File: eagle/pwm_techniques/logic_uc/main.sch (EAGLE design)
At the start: 32 parts, among them IC1 7805T, U1 SN74LS08D, U2 SN74HCT04D

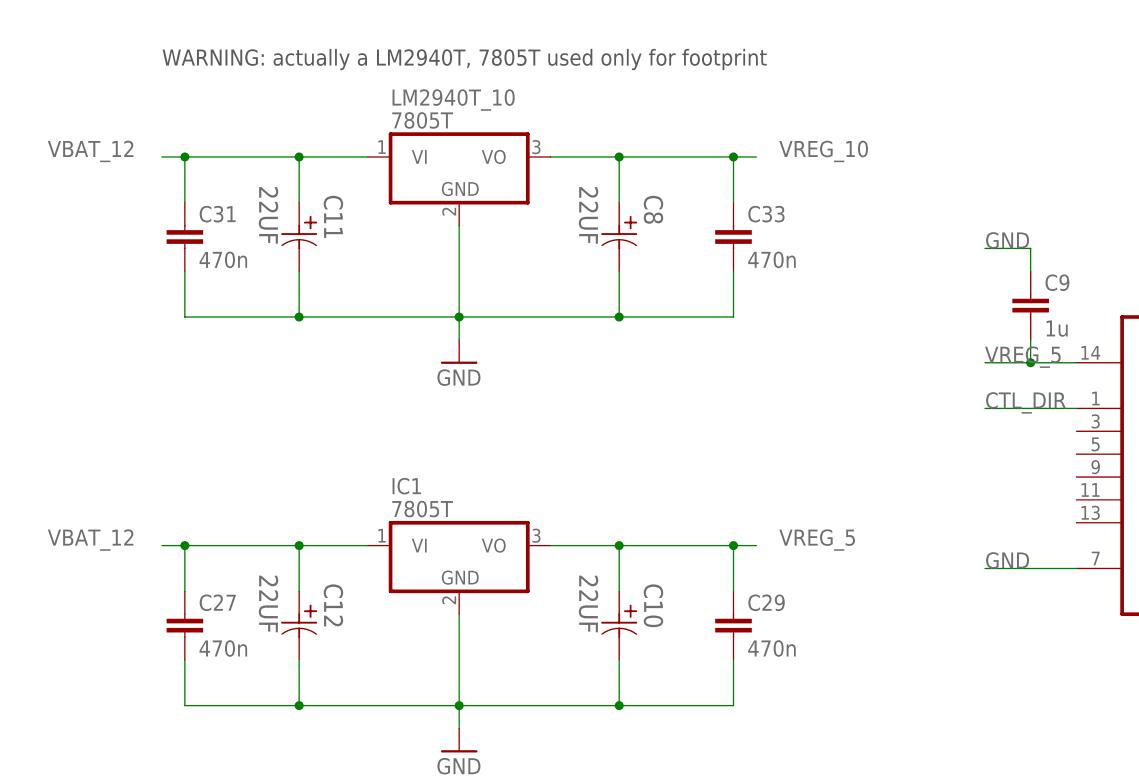
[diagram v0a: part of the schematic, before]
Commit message: [ update ] use SOT223 for LDOs
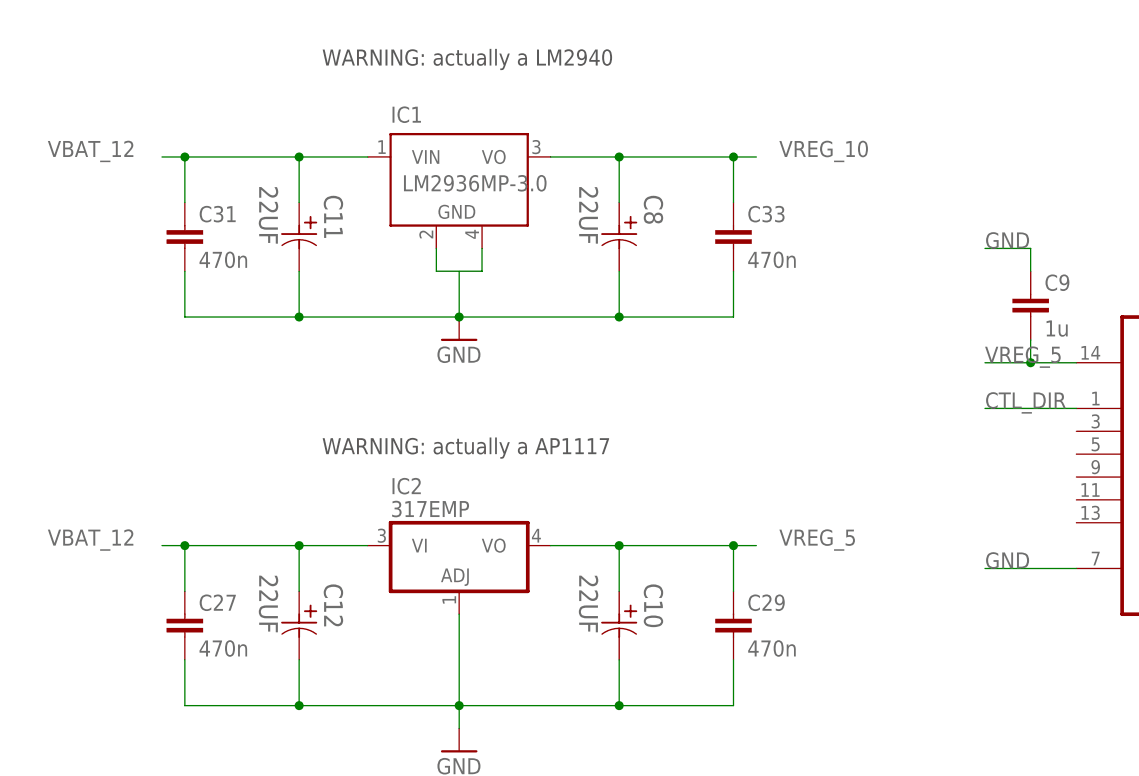
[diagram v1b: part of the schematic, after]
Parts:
- removed LM2940T_10: 7805T, linear:7805T
- added IC2: 317EMP, linear:317EMP
- IC1: value 7805T -> LM2936MP-3.0; device linear:7805T -> national-semiconductor:LM2936MP-3.0
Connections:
- new net N$8: IC1.GND@1, IC1.GND@2
- net GND: now also IC2.ADJ; no longer IC1.GND, LM2940T_10.GND
- net VBAT_12: now also IC1.VIN, IC2.VI; no longer IC1.VI, LM2940T_10.VI
- net VREG_10: now also IC1.VO; no longer LM2940T_10.VO
- net VREG_5: now also IC2.VO; no longer IC1.VO
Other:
- note added: "WARNING: actually a AP1117"
- note added: "WARNING: actually a LM2940"
- note removed: "WARNING: actually a LM2940T, 7805T used only for footprint"
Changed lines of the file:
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@@
 <part name="C33" library="rcl" deviceset="C-EU" device="C1206" value="470n"/>
 <part name="GND4" library="supply1" deviceset="GND" device=""/>
-<part name="IC1" library="linear" deviceset="78*" device="T" technology="05"/>
-<part name="LM2940T_10" library="linear" deviceset="78*" device="T" technology="05"/>
 <part name="BAT_CON" library="con-lstb" deviceset="MA08-1" device=""/>
 <part name="R1" library="rcl" deviceset="R-EU_" device="M1206" value="51"/>
@@
 <part name="C11" library="Panasonic-EEE0_EEE1_EEE2_EEEFC" deviceset="EEE-" device="-CASE-D" technology="1EA220SP" value="22UF"/>
 <part name="C12" library="Panasonic-EEE0_EEE1_EEE2_EEEFC" deviceset="EEE-" device="-CASE-D" technology="1EA220SP" value="22UF"/>
+<part name="IC2" library="linear" deviceset="*317" device="EMP"/>
+<part name="IC1" library="national-semiconductor" deviceset="LM2936MP?*" device="" technology="-3.0"/>
 </parts>
 <sheets>
 <sheet>
 <plain>
-<text x="-101.6" y="43.18" size="1.778" layer="97">WARNING: actually a LM2940T, 7805T used only for footprint</text>
+<text x="-83.82" y="43.18" size="1.778" layer="97">WARNING: actually a LM2940</text>
+<text x="-83.82" y="0" size="1.778" layer="97">WARNING: actually a AP1117</text>
 </plain>
 <instances>
@@
 <instance part="C31" gate="G$1" x="-99.06" y="25.4"/>
 <instance part="C33" gate="G$1" x="-38.1" y="25.4"/>
-<instance part="GND4" gate="1" x="-68.58" y="10.16"/>
-<instance part="IC1" gate="A1" x="-68.58" y="-10.16"/>
-<instance part="LM2940T_10" gate="A1" x="-68.58" y="33.02"/>
+<instance part="GND4" gate="1" x="-68.58" y="12.7"/>
 <instance part="BAT_CON" gate="1" x="-124.46" y="38.1" rot="R180"/>
 <instance part="R1" gate="G$1" x="170.18" y="30.48"/>
@@
 <instance part="C11" gate="A" x="-86.36" y="27.94" rot="R270"/>
 <instance part="C12" gate="A" x="-86.36" y="-15.24" rot="R270"/>
+<instance part="IC2" gate="A1" x="-68.58" y="-12.7"/>
+<instance part="IC1" gate="G$1" x="-68.58" y="30.48"/>
 </instances>
 <busses>
@@
 <wire x1="-38.1" y1="27.94" x2="-38.1" y2="33.02" width="0.1524" layer="91"/>
 <junction x="-38.1" y="33.02"/>
-<pinref part="LM2940T_10" gate="A1" pin="VO"/>
 <pinref part="C8" gate="A" pin="1"/>
+<pinref part="IC1" gate="G$1" pin="VO"/>
 </segment>
 </net>
@@
 <pinref part="GND3" gate="1" pin="GND"/>
 <wire x1="-68.58" y1="-27.94" x2="-68.58" y2="-30.48" width="0.1524" layer="91"/>
-<pinref part="IC1" gate="A1" pin="GND"/>
 <pinref part="C10" gate="A" pin="2"/>
 <pinref part="C12" gate="A" pin="2"/>
+<pinref part="IC2" gate="A1" pin="ADJ"/>
 </segment>
 <segment>
@@
 <wire x1="-86.36" y1="20.32" x2="-86.36" y2="15.24" width="0.1524" layer="91"/>
 <junction x="-86.36" y="15.24"/>
-<wire x1="-68.58" y1="25.4" x2="-68.58" y2="15.24" width="0.1524" layer="91"/>
+<wire x1="-68.58" y1="20.32" x2="-68.58" y2="15.24" width="0.1524" layer="91"/>
 <junction x="-68.58" y="15.24"/>
 <pinref part="GND4" gate="1" pin="GND"/>
-<wire x1="-68.58" y1="15.24" x2="-68.58" y2="12.7" width="0.1524" layer="91"/>
-<pinref part="LM2940T_10" gate="A1" pin="GND"/>
 <pinref part="C11" gate="A" pin="2"/>
 <pinref part="C8" gate="A" pin="2"/>
@@
 <wire x1="-38.1" y1="-15.24" x2="-38.1" y2="-10.16" width="0.1524" layer="91"/>
 <junction x="-38.1" y="-10.16"/>
-<pinref part="IC1" gate="A1" pin="VO"/>
 <pinref part="C10" gate="A" pin="1"/>
+<pinref part="IC2" gate="A1" pin="VO"/>
 </segment>
 </net>
@@
 <wire x1="-86.36" y1="-15.24" x2="-86.36" y2="-10.16" width="0.1524" layer="91"/>
 <junction x="-86.36" y="-10.16"/>
-<pinref part="IC1" gate="A1" pin="VI"/>
 <pinref part="C12" gate="A" pin="1"/>
+<pinref part="IC2" gate="A1" pin="VI"/>
 </segment>
 <segment>
@@
 <wire x1="-86.36" y1="27.94" x2="-86.36" y2="33.02" width="0.1524" layer="91"/>
 <junction x="-86.36" y="33.02"/>
-<pinref part="LM2940T_10" gate="A1" pin="VI"/>
 <pinref part="C11" gate="A" pin="1"/>
+<pinref part="IC1" gate="G$1" pin="VIN"/>
 </segment>
 <segment>
@@
 </segment>
 </net>
+<net name="N$8" class="0">
+<segment>
+<pinref part="IC1" gate="G$1" pin="GND@1"/>
+<wire x1="-71.12" y1="22.86" x2="-71.12" y2="20.32" width="0.1524" layer="91"/>
+<wire x1="-71.12" y1="20.32" x2="-66.04" y2="20.32" width="0.1524" layer="91"/>
+<pinref part="IC1" gate="G$1" pin="GND@2"/>
+<wire x1="-66.04" y1="20.32" x2="-66.04" y2="22.86" width="0.1524" layer="91"/>
+</segment>
+</net>

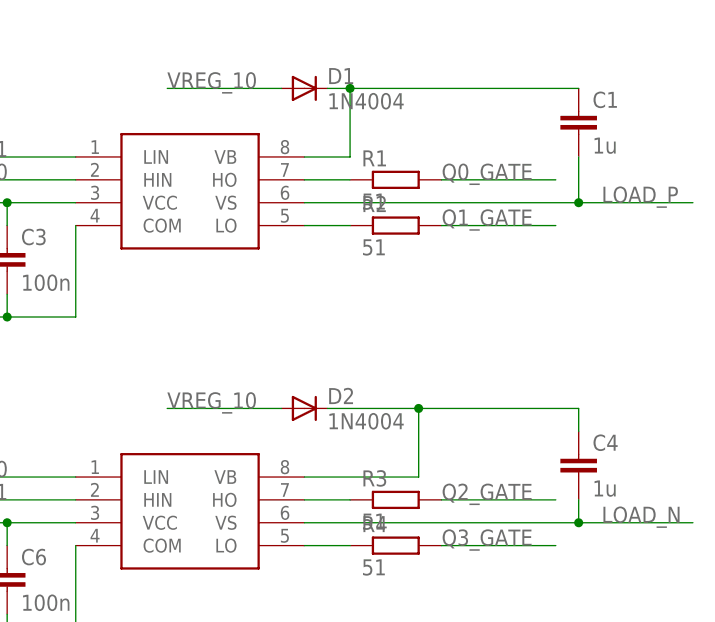
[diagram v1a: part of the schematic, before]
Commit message: [ update ] todo: replace diode package is sod106
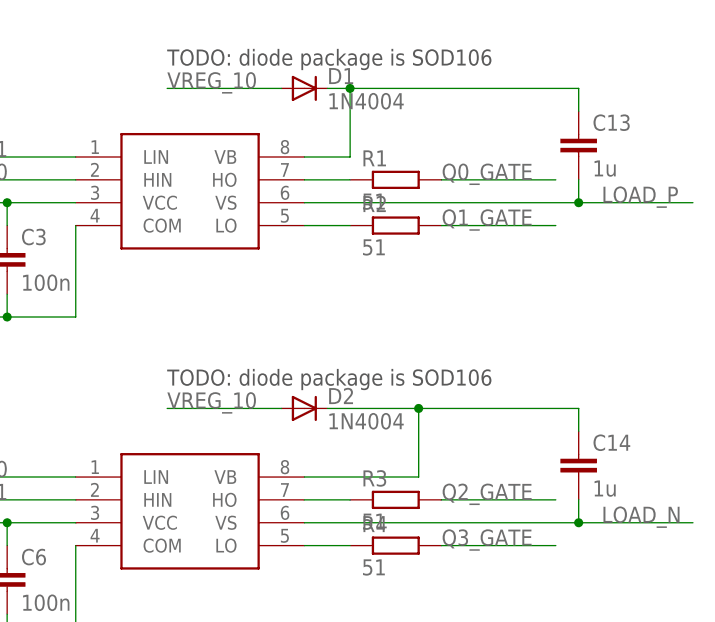
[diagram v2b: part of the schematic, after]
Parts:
- removed C1, C4: 1u, rcl:C-EUC1206
- added C13, C14: 1u, rcl:C-EUC2220K
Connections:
- net LOAD_N: now also C14.2; no longer C4.2
- net LOAD_P: now also C13.2; no longer C1.2
- net N$1: now also C13.1; no longer C1.1
- net N$2: now also C14.1; no longer C4.1
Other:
- note added: "TODO: diode package is SOD106"
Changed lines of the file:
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@@
 <part name="UC_CON" library="con-lstb" deviceset="MA08-1" device=""/>
 <part name="D1" library="diode" deviceset="1N4004" device=""/>
-<part name="C1" library="rcl" deviceset="C-EU" device="C1206" value="1u"/>
 <part name="C2" library="rcl" deviceset="C-EU" device="C1206" value="1u"/>
 <part name="C3" library="rcl" deviceset="C-EU" device="C1206" value="100n"/>
 <part name="IR2304_1" library="ir2304" deviceset="IR2304" device=""/>
 <part name="D2" library="diode" deviceset="1N4004" device=""/>
-<part name="C4" library="rcl" deviceset="C-EU" device="C1206" value="1u"/>
 <part name="C5" library="rcl" deviceset="C-EU" device="C1206" value="1u"/>
 <part name="C6" library="rcl" deviceset="C-EU" device="C1206" value="100n"/>
@@
 <part name="IC2" library="linear" deviceset="*317" device="EMP"/>
 <part name="IC1" library="national-semiconductor" deviceset="LM2936MP?*" device="" technology="-3.0"/>
+<part name="C13" library="rcl" deviceset="C-EU" device="C2220K" value="1u"/>
+<part name="C14" library="rcl" deviceset="C-EU" device="C2220K" value="1u"/>
 </parts>
 <sheets>
@@
 <text x="-83.82" y="43.18" size="1.778" layer="97">WARNING: actually a LM2940</text>
 <text x="-83.82" y="0" size="1.778" layer="97">WARNING: actually a AP1117</text>
+<text x="144.78" y="43.18" size="1.778" layer="97">TODO: diode package is SOD106</text>
+<text x="144.78" y="7.62" size="1.778" layer="97">TODO: diode package is SOD106</text>
 </plain>
 <instances>
@@
 <instance part="UC_CON" gate="1" x="-124.46" y="7.62" rot="R180"/>
 <instance part="D1" gate="1" x="160.02" y="40.64"/>
-<instance part="C1" gate="G$1" x="190.5" y="38.1"/>
 <instance part="C2" gate="G$1" x="119.38" y="22.86"/>
 <instance part="C3" gate="G$1" x="127" y="22.86"/>
 <instance part="IR2304_1" gate="G$1" x="149.86" y="-7.62"/>
 <instance part="D2" gate="1" x="160.02" y="5.08"/>
-<instance part="C4" gate="G$1" x="190.5" y="0"/>
 <instance part="C5" gate="G$1" x="119.38" y="-12.7"/>
 <instance part="C6" gate="G$1" x="127" y="-12.7"/>
@@
 <instance part="IC2" gate="A1" x="-68.58" y="-12.7"/>
 <instance part="IC1" gate="G$1" x="-68.58" y="30.48"/>
+<instance part="C13" gate="G$1" x="190.5" y="35.56"/>
+<instance part="C14" gate="G$1" x="190.5" y="0"/>
 </instances>
 <busses>
@@
 <pinref part="D1" gate="1" pin="C"/>
 <wire x1="165.1" y1="40.64" x2="162.56" y2="40.64" width="0.1524" layer="91"/>
-<pinref part="C1" gate="G$1" pin="1"/>
 <wire x1="165.1" y1="40.64" x2="190.5" y2="40.64" width="0.1524" layer="91"/>
+<wire x1="190.5" y1="40.64" x2="190.5" y2="38.1" width="0.1524" layer="91"/>
 <junction x="165.1" y="40.64"/>
+<pinref part="C13" gate="G$1" pin="1"/>
 </segment>
 </net>
@@
 <pinref part="D2" gate="1" pin="C"/>
 <wire x1="172.72" y1="5.08" x2="162.56" y2="5.08" width="0.1524" layer="91"/>
-<pinref part="C4" gate="G$1" pin="1"/>
 <wire x1="172.72" y1="5.08" x2="190.5" y2="5.08" width="0.1524" layer="91"/>
 <wire x1="190.5" y1="5.08" x2="190.5" y2="2.54" width="0.1524" layer="91"/>
 <junction x="172.72" y="5.08"/>
+<pinref part="C14" gate="G$1" pin="1"/>
 </segment>
 </net>
@@
 <net name="LOAD_P" class="0">
 <segment>
-<pinref part="C1" gate="G$1" pin="2"/>
 <pinref part="IR2304_0" gate="G$1" pin="VS"/>
-<wire x1="190.5" y1="33.02" x2="190.5" y2="27.94" width="0.1524" layer="91"/>
+<wire x1="190.5" y1="30.48" x2="190.5" y2="27.94" width="0.1524" layer="91"/>
 <wire x1="190.5" y1="27.94" x2="160.02" y2="27.94" width="0.1524" layer="91"/>
 <wire x1="190.5" y1="27.94" x2="203.2" y2="27.94" width="0.1524" layer="91"/>
 <junction x="190.5" y="27.94"/>
 <label x="193.04" y="27.94" size="1.778" layer="95"/>
+<pinref part="C13" gate="G$1" pin="2"/>
 </segment>
 <segment>
@@
 <net name="LOAD_N" class="0">
 <segment>
-<pinref part="C4" gate="G$1" pin="2"/>
 <pinref part="IR2304_1" gate="G$1" pin="VS"/>
 <wire x1="190.5" y1="-5.08" x2="190.5" y2="-7.62" width="0.1524" layer="91"/>
@@
 <junction x="190.5" y="-7.62"/>
 <label x="193.04" y="-7.62" size="1.778" layer="95"/>
-</segment>
-<segment>
+<pinref part="C14" gate="G$1" pin="2"/>
+</segment>
+<segment>

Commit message: [ update ] logic_uc main schematics
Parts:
- removed D1, D2: 1N4004, diode:1N4004
- removed UC_CON: (no value), con-lstb:MA08-1
- added U$1, U$2: 1SR154, 1sr154:1SR154
- added U3: ARDUINOR3-DIMENSION, adafruit:ARDUINOR3-DIMENSION
- renumbered HBR_CON to HBR_CON1
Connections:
- net CTL_DIR: now also U3.D2; no longer UC_CON.4
- net CTL_PWM: now also U3.D9; no longer UC_CON.3
- net FB_HBR: now also HBR_CON1.1, U3.A0; no longer HBR_CON1.7, UC_CON.2
- net GND: now also U3.GND1, U3.GND2; no longer UC_CON.5
- net LOAD_N: now also HBR_CON1.6; no longer HBR_CON1.5
- net LOAD_P: now also HBR_CON1.7; no longer HBR_CON1.6
- net N$1: now also U$1.P$2; no longer D1.C
- net N$2: now also U$2.P$2; no longer D2.C
- net Q0_GATE: now also HBR_CON1.2; no longer HBR_CON1.1
- net Q1_GATE: now also HBR_CON1.3; no longer HBR_CON1.2
- net Q2_GATE: now also HBR_CON1.4; no longer HBR_CON1.3
- net Q3_GATE: now also HBR_CON1.5; no longer HBR_CON1.4
- net VREG_10: now also U$1.P$1, U$2.P$1; no longer D1.A, D2.A
- net VREG_5: now also U3.5V
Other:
- note removed: "TODO: diode package is SOD106"
- moved on the sheet: BAT_CON

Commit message: [ update ] logic_uc board routed
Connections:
- net Q0_GATE: now also HBR_CON1.3; no longer HBR_CON1.2
- net Q1_GATE: now also HBR_CON1.2; no longer HBR_CON1.3
- net Q2_GATE: now also HBR_CON1.5; no longer HBR_CON1.4
- net Q3_GATE: now also HBR_CON1.4; no longer HBR_CON1.5
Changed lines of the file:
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@@
 </segment>
 <segment>
-<wire x1="-132.08" y1="-17.78" x2="-152.4" y2="-17.78" width="0.1524" layer="91"/>
-<label x="-152.4" y="-17.78" size="1.778" layer="95"/>
-<pinref part="HBR_CON1" gate="1" pin="2"/>
+<wire x1="-132.08" y1="-20.32" x2="-152.4" y2="-20.32" width="0.1524" layer="91"/>
+<label x="-152.4" y="-20.32" size="1.778" layer="95"/>
+<pinref part="HBR_CON1" gate="1" pin="3"/>
 </segment>
 </net>
@@
 </segment>
 <segment>
-<wire x1="-132.08" y1="-20.32" x2="-152.4" y2="-20.32" width="0.1524" layer="91"/>
-<label x="-152.4" y="-20.32" size="1.778" layer="95"/>
-<pinref part="HBR_CON1" gate="1" pin="3"/>
+<wire x1="-132.08" y1="-17.78" x2="-152.4" y2="-17.78" width="0.1524" layer="91"/>
+<label x="-152.4" y="-17.78" size="1.778" layer="95"/>
+<pinref part="HBR_CON1" gate="1" pin="2"/>
 </segment>
 </net>
@@
 </segment>
 <segment>
-<wire x1="-132.08" y1="-22.86" x2="-152.4" y2="-22.86" width="0.1524" layer="91"/>
-<label x="-152.4" y="-22.86" size="1.778" layer="95"/>
-<pinref part="HBR_CON1" gate="1" pin="4"/>
+<wire x1="-132.08" y1="-25.4" x2="-152.4" y2="-25.4" width="0.1524" layer="91"/>
+<label x="-152.4" y="-25.4" size="1.778" layer="95"/>
+<pinref part="HBR_CON1" gate="1" pin="5"/>
 </segment>
 </net>
@@
 </segment>
 <segment>
-<wire x1="-132.08" y1="-25.4" x2="-152.4" y2="-25.4" width="0.1524" layer="91"/>
-<label x="-152.4" y="-25.4" size="1.778" layer="95"/>
-<pinref part="HBR_CON1" gate="1" pin="5"/>
+<wire x1="-132.08" y1="-22.86" x2="-152.4" y2="-22.86" width="0.1524" layer="91"/>
+<label x="-152.4" y="-22.86" size="1.778" layer="95"/>
+<pinref part="HBR_CON1" gate="1" pin="4"/>
 </segment>
 </net>
